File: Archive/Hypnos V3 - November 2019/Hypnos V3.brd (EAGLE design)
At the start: 25.6 x 52.4 mm, 39 parts, among them Q1 NMOS, Q2 NMOS

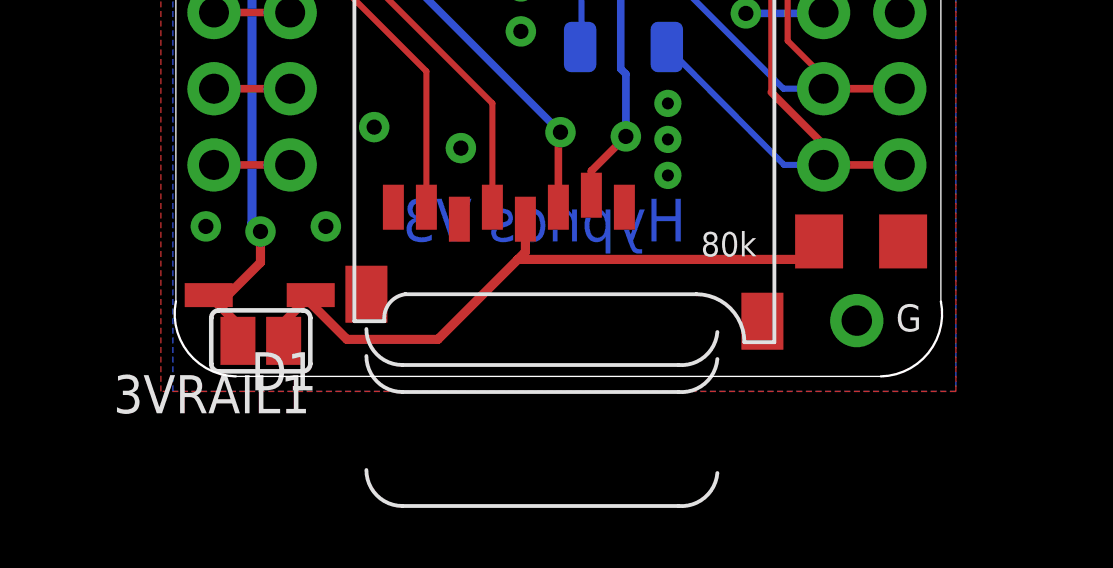
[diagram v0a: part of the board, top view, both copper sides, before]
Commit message: Hypnos V3 hardware fix
Added diode to Hypnos V3 to minimize leaking current from uSD card to 3VRAIL.
Add pdf for schematic Hypnos V2 + Hypnos V3
Updated bill of material to Hypnos V3
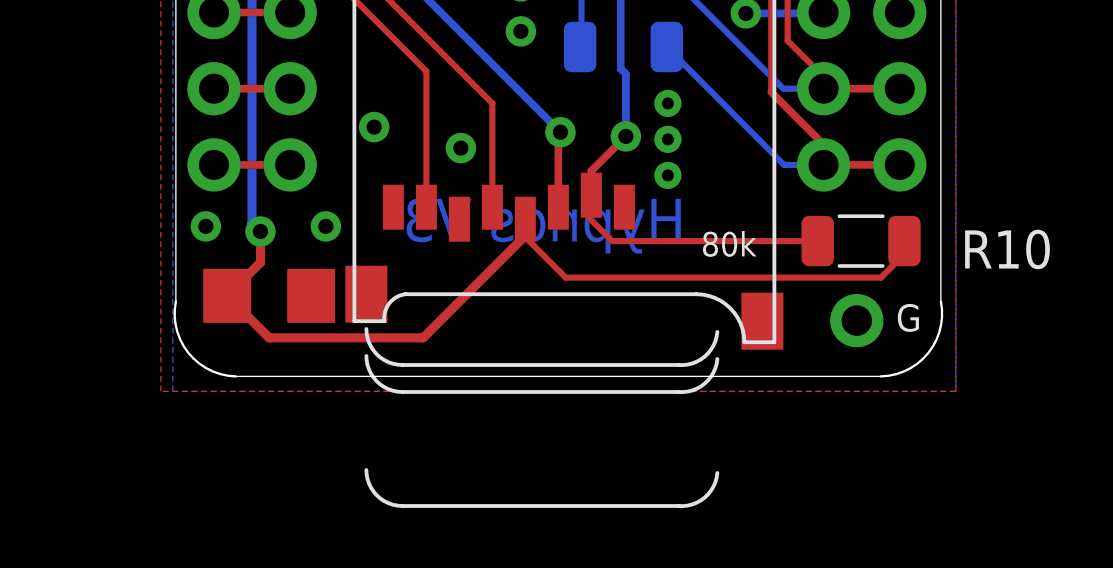
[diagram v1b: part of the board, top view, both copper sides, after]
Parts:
- removed 3VRAIL1: (no value), jumper:SJ
- removed D1: (no value), semicon-smd-ipc:SOD123
- added R10: 30k, Resistor_Capacitor:RES_1206
- moved C1 19.8 mm to (4.11, 3.19)
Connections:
- removed net VDD: 3VRAIL1.1, C1.1, D1.1, MICROSD.4
- net 3VRAIL: now also C1.1, MICROSD.4, R10.1; no longer 3VRAIL1.2, D1.2
- net CS: now also R10.2
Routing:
- net 3VRAIL: track 75.0 -> 99.6 mm
- net VDD: track 22.4 -> 0.00 mm
- net CS: track 13.6 -> 22.2 mm
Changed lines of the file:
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@@
 <attribute name="VALUE" x="14.553" y="17.383" size="1.27" layer="28" rot="MR180"/>
 </element>
-<element name="C1" library="adafruit" library_urn="urn:adsk.eagle:library:420" package="C1206" package3d_urn="urn:adsk.eagle:package:6240335/1" value="100nF" x="23.84" y="5" smashed="yes">
-<attribute name="NAME" x="25.26" y="2.813" size="0.8" layer="51"/>
-<attribute name="VALUE" x="22.57" y="2.587" size="1.27" layer="27"/>
+<element name="C1" library="adafruit" library_urn="urn:adsk.eagle:library:420" package="C1206" package3d_urn="urn:adsk.eagle:package:6240335/1" value="100nF" x="4.11" y="3.185" smashed="yes">
+<attribute name="NAME" x="5.53" y="0.998" size="0.8" layer="51"/>
+<attribute name="VALUE" x="2.84" y="0.772" size="1.27" layer="27"/>
 </element>
 <element name="INT" library="adafruit" library_urn="urn:adsk.eagle:library:420" package="1X01-CLEANBIG" package3d_urn="urn:adsk.eagle:package:6240841/1" value="" x="11.77" y="32.18" smashed="yes">
@@
 </element>
 <element name="MS2" library="adafruit" package="FEATHERWING" package3d_urn="urn:adsk.eagle:package:6240959/1" value="FEATHERWING" x="1" y="52" smashed="yes" rot="R270"/>
+<element name="R10" library="Resistor_Capacitor" library_urn="urn:adsk.eagle:library:11396451" package="RES_1206" package3d_urn="urn:adsk.eagle:package:10872898/2" value="30k" x="23.84" y="5.01" smashed="yes" rot="R180">
+<attribute name="CREATED_BY" value="PCBLayout.com" x="23.84" y="5.01" size="1.778" layer="27" rot="R180" display="off"/>
+<attribute name="DIGIKEY_PART_NUMBER" value="WSLP-.05TR-ND" x="23.84" y="5.01" size="1.778" layer="27" rot="R180" display="off"/>
+<attribute name="MANUFACTURER" value="Vishay Dale" x="23.84" y="5.01" size="1.778" layer="27" rot="R180" display="off"/>
+<attribute name="MPN" value="WSLP1206R0500FEA" x="23.84" y="5.01" size="1.778" layer="27" rot="R180" display="off"/>
+<attribute name="NAME" x="30.237" y="5.367" size="1.27" layer="25" rot="R180"/>
+<attribute name="PACKAGE" value="SMD 1206" x="23.84" y="5.01" size="1.778" layer="27" rot="R180" display="off"/>
+<attribute name="VALUE" x="25.237" y="7.423" size="1.27" layer="27" rot="R180"/>
+</element>
 <element name="RTC_INT" library="SparkFun-Jumpers" library_urn="urn:adsk.eagle:library:528" package="SMT-JUMPER_2_NC_TRACE_SILK" package3d_urn="urn:adsk.eagle:package:39281/1" value="" x="16.88" y="25.33" smashed="yes" rot="MR0">
 <attribute name="VALUE" x="16.88" y="24.187" size="0.6096" layer="28" font="vector" ratio="20" rot="MR0" align="top-center"/>
@@
 <attribute name="NAME" x="8.87" y="49.257" size="0.8128" layer="51" rot="R180"/>
 <attribute name="VALUE" x="10.27" y="52.813" size="1.27" layer="27" rot="R180"/>
-</element>
-<element name="D1" library="semicon-smd-ipc" library_urn="urn:adsk.eagle:library:353" package="SOD123" package3d_urn="urn:adsk.eagle:package:26308/2" value="" x="3.795" y="3.21" smashed="yes" rot="R180">
-<attribute name="NAME" x="5.7" y="1.305" size="1.27" layer="25" rot="R180"/>
-<attribute name="POPULARITY" value="0" x="3.795" y="3.21" size="1.778" layer="27" rot="R180" display="off"/>
-<attribute name="VALUE" x="5.7" y="6.385" size="1.27" layer="27" rot="R180"/>
-</element>
-<element name="3VRAIL1" library="jumper" library_urn="urn:adsk.eagle:library:252" package="SJ" package3d_urn="urn:adsk.eagle:package:15471/1" value="" x="3.83" y="1.685" smashed="yes" rot="R180">
-<attribute name="NAME" x="5.481" y="0.542" size="1.27" layer="25" ratio="10" rot="R180"/>
-<attribute name="VALUE" x="3.4299" y="1.685" size="0.02" layer="27" rot="R180"/>
 </element>
 </elements>
@@
 <wire x1="15.83" y1="17.019934375" x2="15.83" y2="10.75" width="0.254" layer="16"/>
 <wire x1="14.85" y1="6.54" x2="14.7952" y2="6.4852" width="0.2032" layer="1"/>
+<wire x1="14.7952" y1="6.4852" x2="14.7952" y2="5.76375" width="0.2032" layer="1"/>
+<wire x1="14.7952" y1="5.76375" x2="15.54895" y2="5.01" width="0.2032" layer="1"/>
+<contactref element="R10" pad="2"/>
+<wire x1="15.54895" y1="5.01" x2="22.395" y2="5.01" width="0.2032" layer="1"/>
 <wire x1="16.372" y1="19.25" x2="15.83" y2="18.708" width="0.2032" layer="16"/>
 <wire x1="15.83" y1="18.708" x2="15.83" y2="17.019934375" width="0.2032" layer="16"/>
@@
 <contactref element="PMOS2" pad="D"/>
 <contactref element="3V|5V" pad="1"/>
+<contactref element="MICROSD" pad="4"/>
+<wire x1="12.6302" y1="5.7598" x2="12.65" y2="5.74" width="0.254" layer="1"/>
+<wire x1="12.6302" y1="5.17" x2="12.6302" y2="5.7598" width="0.254" layer="1"/>
+<contactref element="C1" pad="1"/>
 <wire x1="12.3" y1="40.5" x2="11.75570625" y2="39.95570625" width="0.4064" layer="1"/>
 <wire x1="11.75570625" y1="39.95570625" x2="7.9643" y2="39.9557" width="0.4064" layer="1"/>
@@
 <wire x1="3.5384" y1="41.8384" x2="3.5384" y2="5.6116" width="0.3048" layer="16"/>
 <wire x1="3.82" y1="5.33" x2="3.5384" y2="5.6116" width="0.3048" layer="16"/>
+<wire x1="9.2452" y1="1.785" x2="12.6302" y2="5.17" width="0.3048" layer="1"/>
 <contactref element="R9" pad="2"/>
 <wire x1="25.147" y1="38" x2="24.072" y2="39.075" width="0.4064" layer="1"/>
 <wire x1="19.905" y1="39.075" x2="24.072" y2="39.075" width="0.4064" layer="1"/>
 <wire x1="18.7771" y1="34.725734375" x2="20" y2="32.985" width="0.2032" layer="1"/>
+<wire x1="2.71" y1="3.185" x2="4.11" y2="1.785" width="0.3048" layer="1"/>
+<wire x1="4.11" y1="1.785" x2="9.2452" y2="1.785" width="0.3048" layer="1"/>
 <wire x1="3.82" y1="5.33" x2="3.82" y2="4.295" width="0.3048" layer="1"/>
+<wire x1="3.82" y1="4.295" x2="2.71" y2="3.185" width="0.3048" layer="1"/>
+<contactref element="R10" pad="1"/>
+<wire x1="12.65" y1="5.74" x2="12.5952" y2="5.6852" width="0.2032" layer="1"/>
+<wire x1="12.5952" y1="5.6852" x2="12.5952" y2="5.19375" width="0.2032" layer="1"/>
+<wire x1="25.285" y1="5.01" x2="25.262" y2="4.55145" width="0.2032" layer="1"/>
+<wire x1="25.262" y1="4.55145" x2="24.50425" y2="3.7937" width="0.2032" layer="1"/>
+<wire x1="12.5952" y1="5.19375" x2="13.99525" y2="3.7937" width="0.2032" layer="1"/>
+<wire x1="13.99525" y1="3.7937" x2="24.50425" y2="3.7937" width="0.2032" layer="1"/>
 <wire x1="19.6121" y1="38" x2="19.6121" y2="38.7821" width="0.4064" layer="1"/>
 <wire x1="16.04620625" y1="36.5964" x2="18.67" y2="36.5964" width="0.4064" layer="1"/>
@@
 <wire x1="18.8079" y1="36.9536625" x2="18.67" y2="36.8157625" width="0.4064" layer="1"/>
 <wire x1="18.67" y1="36.8157625" x2="18.67" y2="36.5964" width="0.4064" layer="1"/>
-<contactref element="3VRAIL1" pad="2"/>
-<contactref element="D1" pad="2"/>
-<wire x1="3.82" y1="4.295" x2="2.735" y2="3.21" width="0.3048" layer="1"/>
-<wire x1="2.735" y1="3.21" x2="2.095" y2="3.21" width="0.3048" layer="1"/>
-<wire x1="2.095" y1="3.21" x2="3.068" y2="2.237" width="0.3048" layer="1"/>
-<wire x1="3.068" y1="2.237" x2="3.068" y2="1.685" width="0.3048" layer="1"/>
 </signal>
 <signal name="5VRAIL">
@@
 <wire x1="13.58535" y1="50.84415" x2="14.7895" y2="49.64" width="0.2032" layer="1"/>
 </signal>
-<signal name="VDD">
-<contactref element="C1" pad="1"/>
-<contactref element="D1" pad="1"/>
-<contactref element="3VRAIL1" pad="1"/>
-<contactref element="MICROSD" pad="4"/>
-<wire x1="4.592" y1="1.685" x2="4.592" y2="2.307" width="0.3048" layer="1"/>
-<wire x1="4.592" y1="2.307" x2="5.495" y2="3.21" width="0.3048" layer="1"/>
-<wire x1="6.70270625" y1="1.7344" x2="5.495" y2="2.94210625" width="0.3048" layer="1"/>
-<wire x1="5.495" y1="3.21" x2="5.495" y2="2.94210625" width="0.3048" layer="1"/>
-<wire x1="6.70270625" y1="1.7344" x2="9.7344" y2="1.7344" width="0.3048" layer="1"/>
-<wire x1="12.65" y1="4.65" x2="12.65" y2="5.74" width="0.3048" layer="1"/>
-<wire x1="9.7344" y1="1.7344" x2="12.4" y2="4.4" width="0.3048" layer="1"/>
-<wire x1="12.4" y1="4.4" x2="12.65" y2="4.65" width="0.3048" layer="1"/>
-<wire x1="22.44" y1="5" x2="21.84" y2="4.4" width="0.3048" layer="1"/>
-<wire x1="21.84" y1="4.4" x2="12.4" y2="4.4" width="0.3048" layer="1"/>
-</signal>
 </signals>
